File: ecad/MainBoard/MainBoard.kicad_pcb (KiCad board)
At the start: 2 copper layers, 34.6 x 88.7 mm, 44 parts, among them IC1 RC4558, J1 ACJM-HHDR, J2 ACJM-HHDR, J3 PJ-102A, Q1 2N4424, Q2 2N4424, SW1 FS57003PLT2B2M2QE

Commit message: Board 1v0
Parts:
- added G***: LOGO, screaming-panda:Panda_Logo, B.Cu at (90.2, 78.8)
- added REF**: KiCad-Logo2_5mm_SilkScreen, Symbol:KiCad-Logo2_5mm_SilkScreen, B.Cu at (87.8, 98.3)
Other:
- board text added: "9/2021"
- board text added: "John McAvoy"
- board text added: "Main Board"
- board text added: "Screaming Panda 1v0"

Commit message: Remove j-mcavoy kicad lib submodule
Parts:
- removed G***: LOGO, screaming-panda:Panda_Logo
- removed REF**: KiCad-Logo2_5mm_SilkScreen, Symbol:KiCad-Logo2_5mm_SilkScreen
- C12: footprint screaming-panda:CAPPRD250W55D655H1220 -> j-mcavoy:CAPPRD250W55D655H1220
- J1, J2: footprint screaming-panda:ACJM-HHDR -> j-mcavoy:ACJM-HHDR
- J3: footprint screaming-panda:Barrel_Jack_5.5mmODx2.1mmID_PJ-102A -> j-mcavoy:Barrel_Jack_5.5mmODx2.1mmID_PJ-102A
- Q1, Q2: footprint digikey-footprints:TO-92-3_Formed_Leads -> j-mcavoy:TO-92-3_Formed_Leads
- R19, R20, R21: footprint screaming-panda:75160-195-03LF -> j-mcavoy:75160-195-03LF
- SW1: footprint screaming-panda:SW_PUSH_E-Switch_FS57003PLT_3PDT -> j-mcavoy:SW_PUSH_E-Switch_FS57003PLT_3PDT
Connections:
- net /tone/IN renamed /drive/OUT
- net /volume/IN renamed /tone/OUT
- R19 pad 1: (no net) -> unconnected-(R19-Pad1)
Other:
- outline, holes or cut-outs redrawn
- net class Default removed

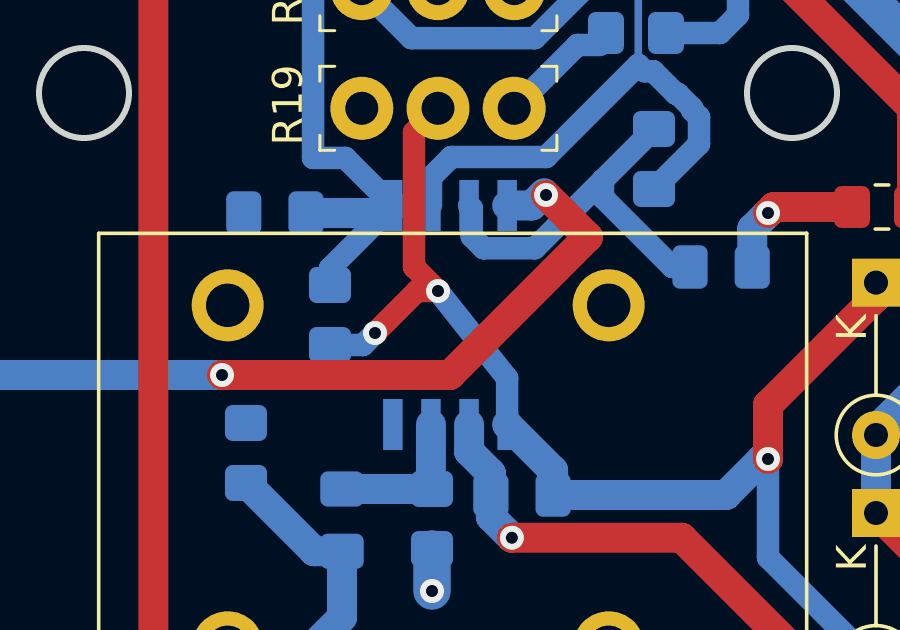
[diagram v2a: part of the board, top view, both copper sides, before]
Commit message: Update libraries to j-mcavoy kicad library
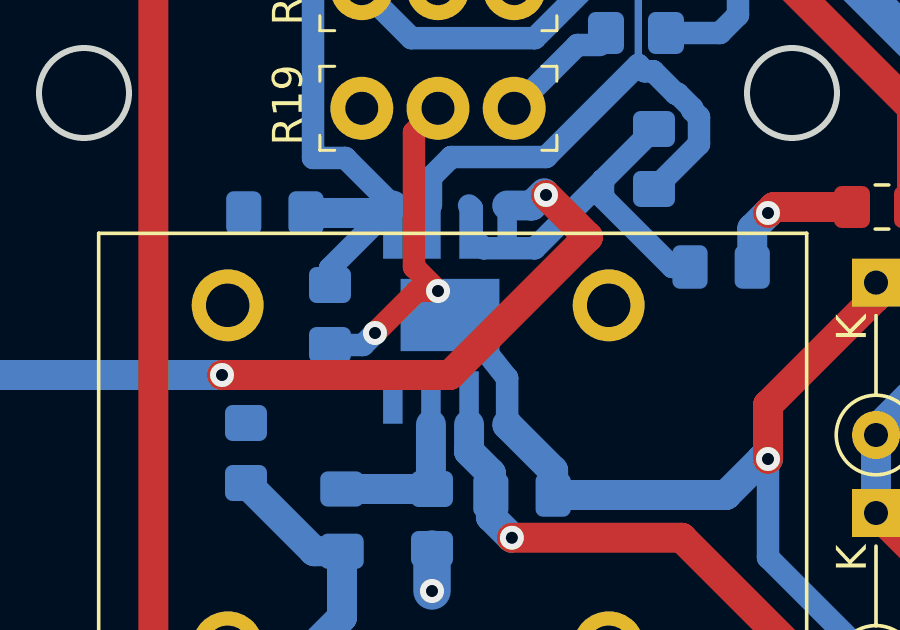
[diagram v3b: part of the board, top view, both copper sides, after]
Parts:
- IC1: footprint digikey-footprints:SOIC-8_W5.6mm -> j-mcavoy:SOIC-8-1EP_W3.9mm
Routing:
- net /tone/OUT: track 13.4 -> 0.00 mm
- net +9V: track 135.2 -> 148.6 mm
